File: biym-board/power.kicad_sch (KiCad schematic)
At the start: 4 parts, among them J1 HEADER_01X02_JST_SH_SMD_VERTI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, Q1 MOSFET-N-CH-EN, Q2 MOSFET-P-CH-EN

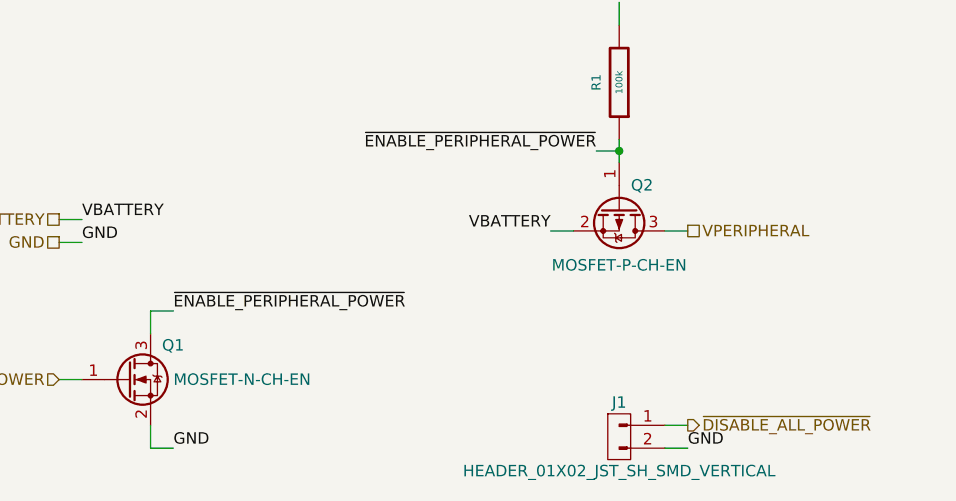
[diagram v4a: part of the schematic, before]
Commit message: Initial driver wiring
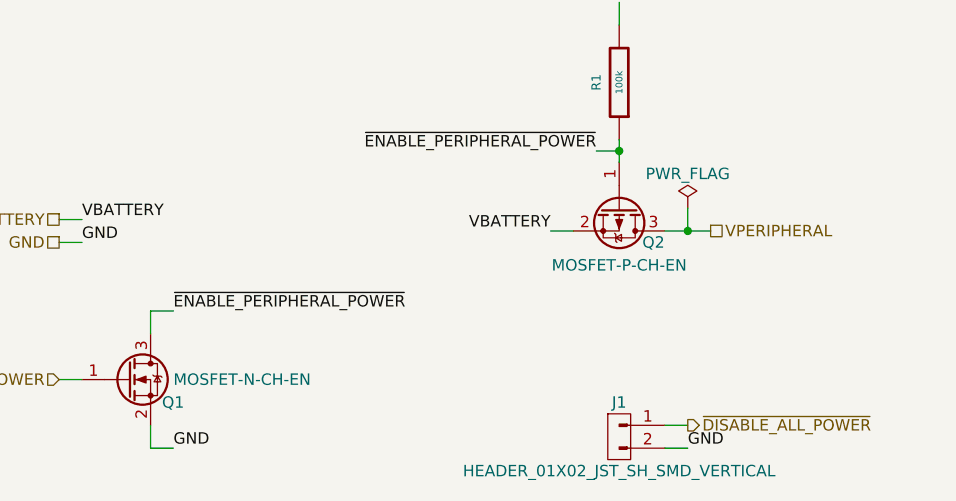
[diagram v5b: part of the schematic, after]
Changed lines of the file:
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@@
     (rev "0.1")
+  )
+  (junction (at 171.45 96.52) (diameter 0) (color 0 0 0 0)
   )
   (junction (at 163.83 87.63) (diameter 0) (color 0 0 0 0)
@@
     (stroke (width 0) (type default) (color 0 0 0 0))
   )
+  (wire (pts (xy 171.45 93.98) (xy 171.45 96.52))
+    (stroke (width 0) (type default) (color 0 0 0 0))
+  )
   (wire (pts (xy 168.91 118.11) (xy 171.45 118.11))
     (stroke (width 0) (type default) (color 0 0 0 0))
@@
   )
   (wire (pts (xy 101.6 113.03) (xy 104.14 113.03))
+    (stroke (width 0) (type default) (color 0 0 0 0))
+  )
+  (wire (pts (xy 171.45 96.52) (xy 173.99 96.52))
     (stroke (width 0) (type default) (color 0 0 0 0))
   )
@@
     (effects (font (size 1.27 1.27)) (justify left bottom))
   )
-  (hierarchical_label "VPERIPHERAL" (shape passive) (at 171.45 96.52 0)
+  (hierarchical_label "VPERIPHERAL" (shape passive) (at 173.99 96.52 0)
     (effects (font (size 1.27 1.27)) (justify left))
   )
@@
   (symbol (lib_id "Janelia:MOSFET-P-CH-EN-DMP2045UQ-7") (at 163.83 93.98 270) (unit 1)
     (in_bom yes) (on_board yes)
-    (property "Reference" "Q2" (id 0) (at 166.37 91.44 90))
+    (property "Reference" "Q2" (id 0) (at 167.64 97.79 90))
     (property "Value" "MOSFET-P-CH-EN" (id 1) (at 163.83 100.33 90))
     (property "Footprint" "Janelia:SOT-23-3" (id 2) (at 161.925 99.06 0)
@@
     (pin "3")
   )
+  (symbol (lib_id "power:PWR_FLAG") (at 171.45 93.98 0) (unit 1)
+    (in_bom yes) (on_board yes)
+    (property "Reference" "#FLG0101" (id 0) (at 171.45 92.075 0)
+      (effects (font (size 1.27 1.27)) hide)
+    )
+    (property "Value" "PWR_FLAG" (id 1) (at 171.45 90.17 0))
+    (property "Footprint" "" (id 2) (at 171.45 93.98 0)
+      (effects (font (size 1.27 1.27)) hide)
+    )
+    (property "Datasheet" "~" (id 3) (at 171.45 93.98 0)
+      (effects (font (size 1.27 1.27)) hide)
+    )
+    (pin "1")
+  )
   (symbol (lib_id "Janelia:MOSFET-N-CH-EN-DMG2302UKQ-7") (at 109.22 113.03 0) (unit 1)
     (in_bom yes) (on_board yes)
-    (property "Reference" "Q1" (id 0) (at 113.03 109.22 0)
+    (property "Reference" "Q1" (id 0) (at 113.03 115.57 0)
       (effects (font (size 1.27 1.27)) (justify left))
     )

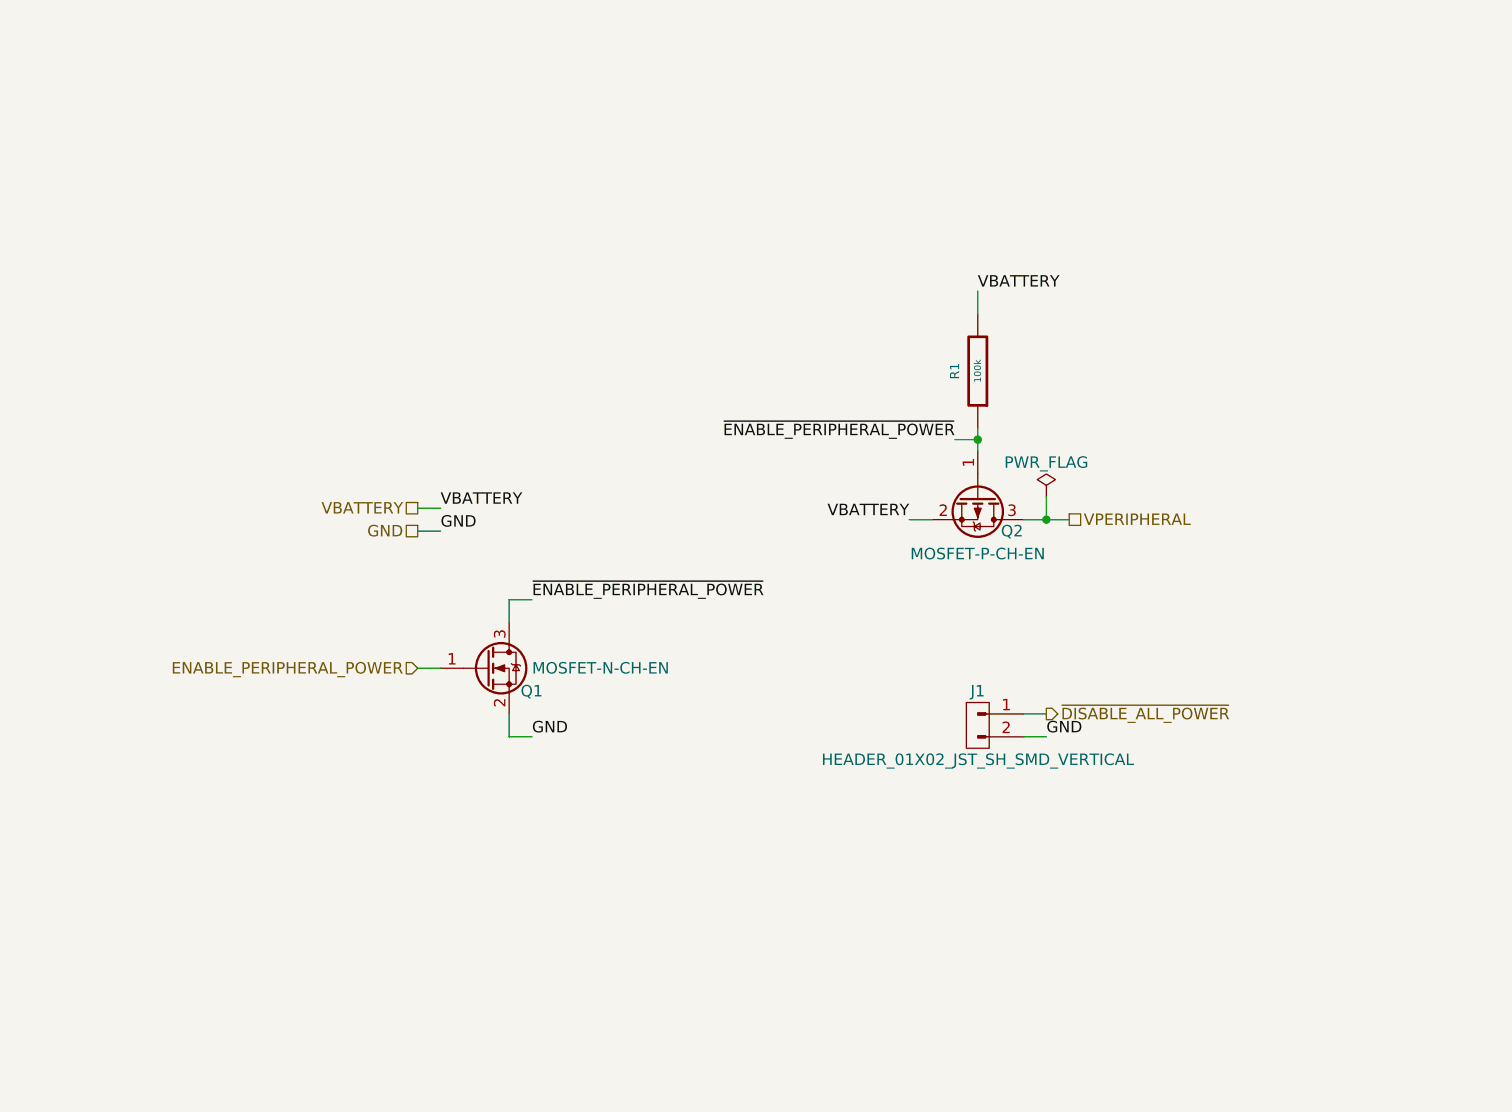
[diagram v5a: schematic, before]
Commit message: Add boosted voltage
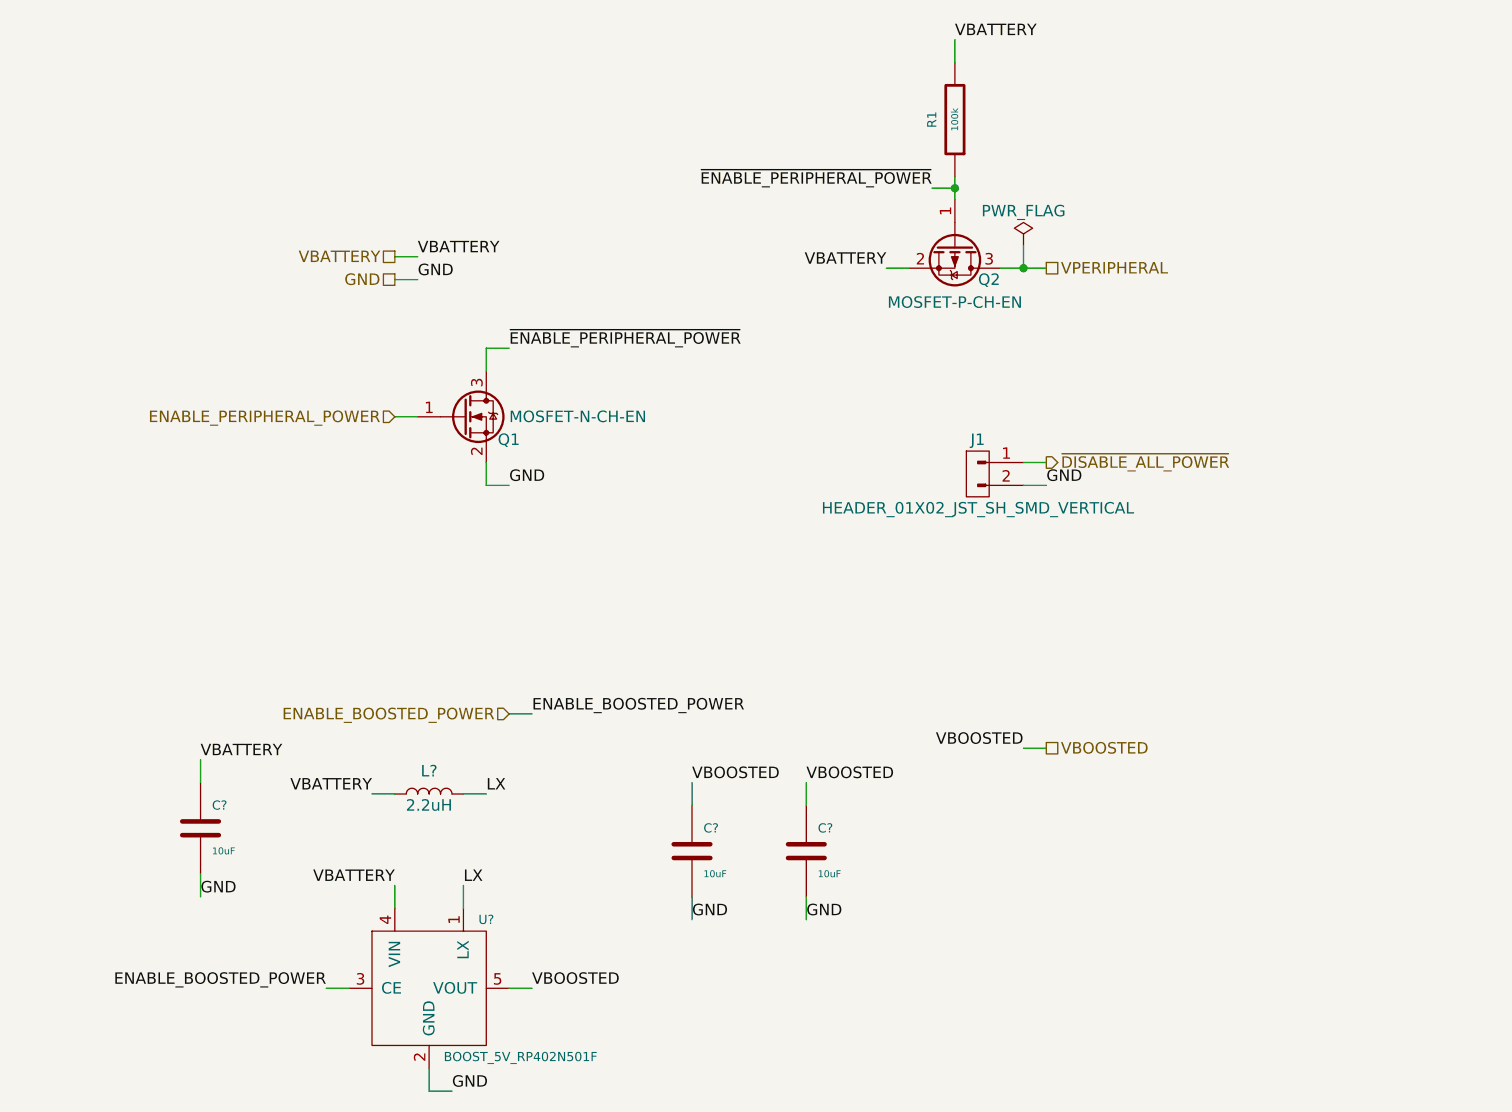
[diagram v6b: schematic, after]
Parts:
- added C? (x3): 10uF, Janelia:SM0603, symbol Janelia:10uF_0603
- added L?: 2.2uH, Janelia:INDUCTOR_VLS_HBX, symbol Janelia:L_2.2uH_3A
- added U?: BOOST_5V_RP402N501F, Janelia:SOT-23-5, symbol Janelia:BOOST_5V_RP402N501F
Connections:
- net GND: now also C?.2, C?.2, C?.2, U?.2 (GND)
- net VBATTERY: now also C?.1, L?.1, U?.4 (VIN)
- new net ENABLE_BOOSTED_POWER: U?.3 (CE)
- new net LX: L?.2, U?.1 (LX)
- new net VBOOSTED: C?.1, C?.1, U?.5 (VOUT)
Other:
- moved on the sheet: J1, Q1, Q2, R1

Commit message: output -> servo
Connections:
- net ENABLE_BOOSTED_POWER renamed ENABLE_BOOSTED
- net ENABLE_PERIPHERAL_POWER renamed ENABLE_PERIPHERAL
- net ~{DISABLE_ALL_POWER} renamed ~{DISABLE_ALL}
- net ~{ENABLE_PERIPHERAL_POWER} renamed ~{ENABLE_PERIPHERAL}
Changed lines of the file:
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@@
     (effects (font (size 1.27 1.27)) (justify left bottom))
   )
-  (label "ENABLE_BOOSTED_POWER" (at 91.44 148.59 180)
+  (label "ENABLE_BOOSTED" (at 91.44 148.59 180)
     (effects (font (size 1.27 1.27)) (justify right bottom))
   )
@@
     (effects (font (size 1.27 1.27)) (justify left bottom))
   )
-  (label "~{ENABLE_PERIPHERAL_POWER}" (at 158.75 59.69 180)
+  (label "~{ENABLE_PERIPHERAL}" (at 158.75 59.69 180)
     (effects (font (size 1.27 1.27)) (justify right bottom))
   )
@@
     (effects (font (size 1.27 1.27)) (justify right bottom))
   )
-  (label "~{ENABLE_PERIPHERAL_POWER}" (at 111.76 77.47 0)
+  (label "~{ENABLE_PERIPHERAL}" (at 111.76 77.47 0)
     (effects (font (size 1.27 1.27)) (justify left bottom))
   )
@@
     (effects (font (size 1.27 1.27)) (justify left bottom))
   )
-  (label "ENABLE_BOOSTED_POWER" (at 114.3 118.11 0)
+  (label "ENABLE_BOOSTED" (at 114.3 118.11 0)
     (effects (font (size 1.27 1.27)) (justify left bottom))
   )
@@
     (effects (font (size 1.27 1.27)) (justify left))
   )
-  (hierarchical_label "ENABLE_BOOSTED_POWER" (shape input) (at 111.76 118.11 180)
+  (hierarchical_label "ENABLE_BOOSTED" (shape input) (at 111.76 118.11 180)
     (effects (font (size 1.27 1.27)) (justify right))
   )
-  (hierarchical_label "ENABLE_PERIPHERAL_POWER" (shape input) (at 99.06 85.09 180)
+  (hierarchical_label "ENABLE_PERIPHERAL" (shape input) (at 99.06 85.09 180)
     (effects (font (size 1.27 1.27)) (justify right))
   )
-  (hierarchical_label "~{DISABLE_ALL_POWER}" (shape output) (at 171.45 90.17 0)
+  (hierarchical_label "~{DISABLE_ALL}" (shape output) (at 171.45 90.17 0)
     (effects (font (size 1.27 1.27)) (justify left))
   )

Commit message: Finished v0.1 of schematic
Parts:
- removed C? (x3): 10uF, Janelia:SM0603, symbol Janelia:10uF_0603
- removed R1: 100k, Janelia:SM0402, symbol Janelia:100k_0402
- added C1, C2, C3: C_10uF_0603, Janelia:SM0603, symbol Janelia:C_10uF_0603
- added R1: R_110k_0402, Janelia:SM0402, symbol Janelia:R_110k_0402
- gave numbers to parts that had none: 2
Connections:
- net GND: now also C1.2, C2.2, C3.2
- net VBATTERY: now also C1.1, R1.1
- net VBOOSTED: now also C2.1, C3.1
- net ~{ENABLE_PERIPHERAL}: now also R1.2
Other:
- company: (none) -> Peter Polidoro
